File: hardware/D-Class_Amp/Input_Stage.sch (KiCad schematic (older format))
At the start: 19 parts

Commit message: edited input filter ground, created schematic for the SPWM generator
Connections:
- net labels removed: GND
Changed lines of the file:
@@
 $Descr A4 11693 8268
 encoding utf-8
-Sheet 1 1
+Sheet 2 5
 Title "D-Class Input Filter"
 Date "2021-07-31"
@@
 	8250 3600 8250 3550
 Connection ~ 8250 3600
-$Comp
-L power:GND #PWR?
-U 1 1 610999BC
-P 7550 3950
-F 0 "#PWR?" H 7550 3700 50  0001 C CNN
-F 1 "GND" H 7555 3777 50  0000 C CNN
-F 2 "" H 7550 3950 50  0001 C CNN
-F 3 "" H 7550 3950 50  0001 C CNN
-	1    7550 3950
-	1    0    0    -1
-$EndComp
-$Comp
-L power:GND #PWR?
-U 1 1 61099C7B
-P 8250 3950
-F 0 "#PWR?" H 8250 3700 50  0001 C CNN
-F 1 "GND" H 8255 3777 50  0000 C CNN
-F 2 "" H 8250 3950 50  0001 C CNN
-F 3 "" H 8250 3950 50  0001 C CNN
-	1    8250 3950
-	1    0    0    -1
-$EndComp
 Text HLabel 2600 3200 0    50   Input ~ 0
 SIG_IN
@@
 Text Label 3900 4650 0    50   ~ 0
 C_OUT
-Text HLabel 6650 4550 2    50   Input ~ 0
+Text HLabel 6650 4550 2    50   Output ~ 0
 FILT_OUT
 Wire Wire Line
@@
 	1    0    0    -1
 $EndComp
+$Comp
+L power:GNDS #PWR?
+U 1 1 61096DF3
+P 7550 3950
+F 0 "#PWR?" H 7550 3700 50  0001 C CNN
+F 1 "GNDS" H 7555 3777 50  0000 C CNN
+F 2 "" H 7550 3950 50  0001 C CNN
+F 3 "" H 7550 3950 50  0001 C CNN
+	1    7550 3950
+	1    0    0    -1
+$EndComp
+$Comp
+L power:GNDS #PWR?
+U 1 1 61097302
+P 8250 3950
+F 0 "#PWR?" H 8250 3700 50  0001 C CNN
+F 1 "GNDS" H 8255 3777 50  0000 C CNN
+F 2 "" H 8250 3950 50  0001 C CNN
+F 3 "" H 8250 3950 50  0001 C CNN
+	1    8250 3950
+	1    0    0    -1
+$EndComp

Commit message: edits
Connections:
- net labels added: +5V, -5V
- net labels removed: +3.3V, -3V3
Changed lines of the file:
@@
-$EndComp
-$Comp
-L power:+3.3V #PWR?
-U 1 1 610DB258
-P 8250 3550
-F 0 "#PWR?" H 8250 3400 50  0001 C CNN
-F 1 "+3.3V" H 8265 3723 50  0000 C CNN
-F 2 "" H 8250 3550 50  0001 C CNN
-F 3 "" H 8250 3550 50  0001 C CNN
-	1    8250 3550
-	1    0    0    -1
-$EndComp
-$Comp
-L power:-3V3 #PWR?
-U 1 1 610DB7DD
-P 7550 3550
-F 0 "#PWR?" H 7550 3650 50  0001 C CNN
-F 1 "-3V3" H 7565 3723 50  0000 C CNN
-F 2 "" H 7550 3550 50  0001 C CNN
-F 3 "" H 7550 3550 50  0001 C CNN
-	1    7550 3550
-	1    0    0    -1
 $EndComp
 $Comp
@@
 	1    0    0    -1
 $EndComp
+$Comp
+L power:-5V #PWR?
+U 1 1 611D5337
+P 7550 3550
+F 0 "#PWR?" H 7550 3650 50  0001 C CNN
+F 1 "-5V" H 7565 3723 50  0000 C CNN
+F 2 "" H 7550 3550 50  0001 C CNN
+F 3 "" H 7550 3550 50  0001 C CNN
+	1    7550 3550
+	1    0    0    -1
+$EndComp
+$Comp
+L power:+5V #PWR?
+U 1 1 611D5A3A
+P 8250 3550
+F 0 "#PWR?" H 8250 3400 50  0001 C CNN
+F 1 "+5V" H 8265 3723 50  0000 C CNN
+F 2 "" H 8250 3550 50  0001 C CNN
+F 3 "" H 8250 3550 50  0001 C CNN
+	1    8250 3550
+	1    0    0    -1
+$EndComp

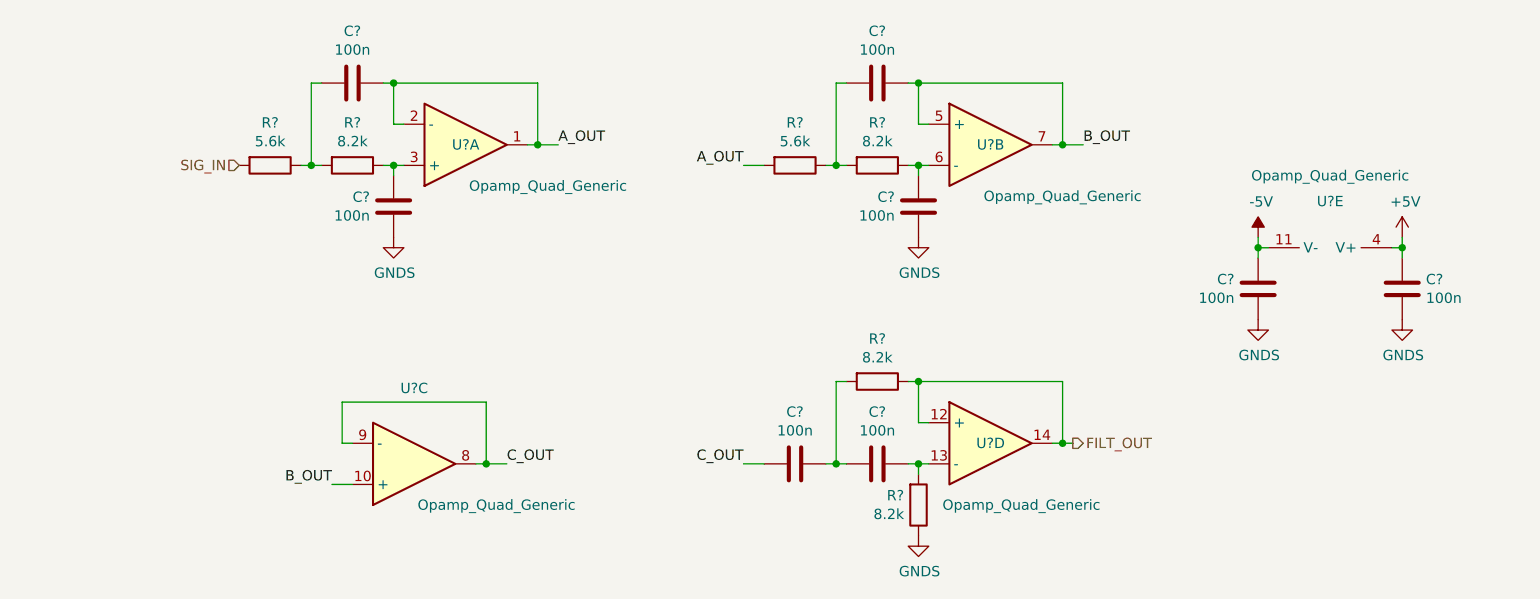
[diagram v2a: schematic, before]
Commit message: Selected Op-Amp for input stage and labelled parts
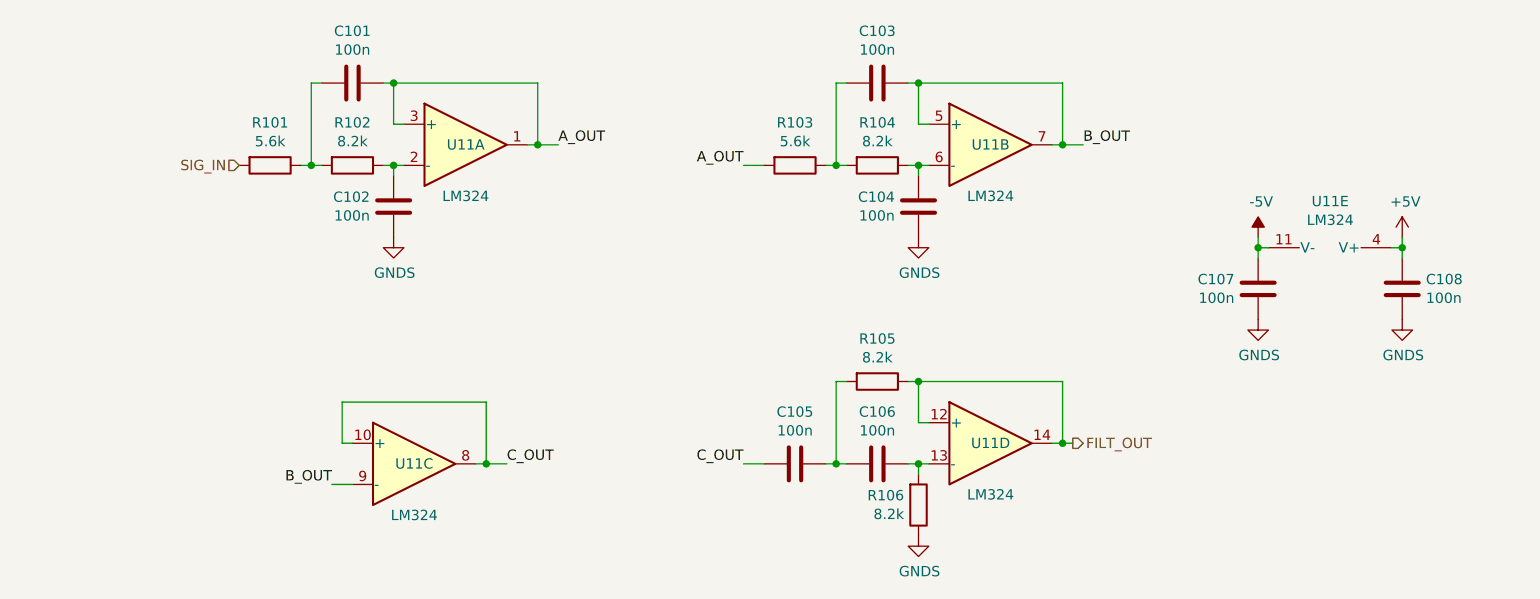
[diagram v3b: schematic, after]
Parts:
- removed U? (x5): Opamp_Quad_Generic, symbol Device:Opamp_Quad_Generic
- added U11: LM324, symbol Amplifier_Operational:LM324
- gave numbers to parts that had none: 14
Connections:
- net +5V: now also U11.4 (V+)
- net -5V: now also U11.11 (V-)
- net A_OUT: now also U11.1, U11.3 (+)
- net B_OUT: now also U11.5 (+), U11.7, U11.9 (-)
- net C_OUT: now also U11.10 (+), U11.8
- net FILT_OUT: now also U11.12 (+), U11.14
- net at C102.2, R102.1: now also U11.2 (-)
- net at C104.2, R104.1: now also U11.6 (-)
- net at C106.1, R106.2: now also U11.13 (-)
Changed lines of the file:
@@
 $Descr A4 11693 8268
 encoding utf-8
-Sheet 2 5
+Sheet 1 1
 Title "D-Class Input Filter"
 Date "2021-07-31"
@@
 $EndDescr
 $Comp
-L Device:Opamp_Quad_Generic U?
-U 2 1 6104ADDA
-P 6250 3100
-F 0 "U?" H 6250 3100 50  0000 C CNN
-F 1 "Opamp_Quad_Generic" H 6600 2850 50  0000 C CNN
-F 2 "" H 6250 3100 50  0001 C CNN
-F 3 "~" H 6250 3100 50  0001 C CNN
-	2    6250 3100
-	1    0    0    -1
-$EndComp
-$Comp
-L Device:Opamp_Quad_Generic U?
-U 3 1 6104B460
-P 3450 4650
-F 0 "U?" H 3450 4283 50  0000 C CNN
-F 1 "Opamp_Quad_Generic" H 3850 4850 50  0000 C CNN
-F 2 "" H 3450 4650 50  0001 C CNN
-F 3 "~" H 3450 4650 50  0001 C CNN
-	3    3450 4650
-	1    0    0    1
-$EndComp
-$Comp
-L Device:Opamp_Quad_Generic U?
-U 4 1 6104BA16
-P 6250 4550
-F 0 "U?" H 6250 4550 50  0000 C CNN
-F 1 "Opamp_Quad_Generic" H 6400 4250 50  0000 C CNN
-F 2 "" H 6250 4550 50  0001 C CNN
-F 3 "~" H 6250 4550 50  0001 C CNN
-	4    6250 4550
-	1    0    0    -1
-$EndComp
-$Comp
-L Device:Opamp_Quad_Generic U?
-U 5 1 6104C141
-P 7900 3700
-F 0 "U?" V 7575 3700 50  0000 C CNN
-F 1 "Opamp_Quad_Generic" V 7450 3700 50  0000 C CNN
-F 2 "" H 7900 3700 50  0001 C CNN
-F 3 "~" H 7900 3700 50  0001 C CNN
-	5    7900 3700
-	0    1    1    0
-$EndComp
-$Comp
-L Device:Opamp_Quad_Generic U?
-U 1 1 6104A90C
-P 3700 3100
-F 0 "U?" H 3700 3100 50  0000 C CNN
-F 1 "Opamp_Quad_Generic" H 4100 3300 50  0000 C CNN
-F 2 "" H 3700 3100 50  0001 C CNN
-F 3 "~" H 3700 3100 50  0001 C CNN
-	1    3700 3100
-	1    0    0    1
-$EndComp
-$Comp
-L Device:R R?
+L Device:R R101
 U 1 1 61051550
 P 2750 3200
-F 0 "R?" V 2543 3200 50  0000 C CNN
+F 0 "R101" V 2543 3200 50  0000 C CNN
 F 1 "5.6k" V 2634 3200 50  0000 C CNN
 F 2 "" V 2680 3200 50  0001 C CNN
@@
 $EndComp
 $Comp
-L Device:C C?
+L Device:C C102
 U 1 1 610518F4
 P 3350 3400
-F 0 "C?" H 3235 3354 50  0000 R CNN
+F 0 "C102" H 3235 3354 50  0000 R CNN
 F 1 "100n" H 3235 3445 50  0000 R CNN
 F 2 "" H 3388 3250 50  0001 C CNN
@@
 $EndComp
 $Comp
-L Device:R R?
+L Device:R R102
 U 1 1 61052760
 P 3150 3200
-F 0 "R?" V 2943 3200 50  0000 C CNN
+F 0 "R102" V 2943 3200 50  0000 C CNN
 F 1 "8.2k" V 3034 3200 50  0000 C CNN
 F 2 "" V 3080 3200 50  0001 C CNN
@@
 	4050 3100 4000 3100
 $Comp
-L Device:C C?
+L Device:C C101
 U 1 1 6105C4D1
 P 3150 2800
-F 0 "C?" V 2898 2800 50  0000 C CNN
+F 0 "C101" V 2898 2800 50  0000 C CNN
 F 1 "100n" V 2989 2800 50  0000 C CNN
 F 2 "" H 3188 2650 50  0001 C CNN
@@
 	3350 2800 4050 2800
 $Comp
-L Device:R R?
+L Device:R R103
 U 1 1 6105F15E
 P 5300 3200
-F 0 "R?" V 5093 3200 50  0000 C CNN
+F 0 "R103" V 5093 3200 50  0000 C CNN
 F 1 "5.6k" V 5184 3200 50  0000 C CNN
 F 2 "" V 5230 3200 50  0001 C CNN
@@
 $EndComp
 $Comp
-L Device:C C?
+L Device:C C104
 U 1 1 6105F164
 P 5900 3400
-F 0 "C?" H 5785 3354 50  0000 R CNN
+F 0 "C104" H 5785 3354 50  0000 R CNN
 F 1 "100n" H 5785 3445 50  0000 R CNN
 F 2 "" H 5938 3250 50  0001 C CNN
@@
 $EndComp
 $Comp
-L Device:R R?
+L Device:R R104
 U 1 1 6105F16A
 P 5700 3200
-F 0 "R?" V 5493 3200 50  0000 C CNN
+F 0 "R104" V 5493 3200 50  0000 C CNN
 F 1 "8.2k" V 5584 3200 50  0000 C CNN
 F 2 "" V 5630 3200 50  0001 C CNN
@@
 	6600 3100 6550 3100
 $Comp
-L Device:C C?
+L Device:C C103
 U 1 1 6105F17C
 P 5700 2800
-F 0 "C?" V 5448 2800 50  0000 C CNN
+F 0 "C103" V 5448 2800 50  0000 C CNN
 F 1 "100n" V 5539 2800 50  0000 C CNN
 F 2 "" H 5738 2650 50  0001 C CNN
@@
 	3800 4650 3750 4650
 $Comp
-L Device:R R?
+L Device:R R106
 U 1 1 6106C181
 P 5900 4850
-F 0 "R?" H 5830 4804 50  0000 R CNN
+F 0 "R106" H 5830 4804 50  0000 R CNN
 F 1 "8.2k" H 5830 4895 50  0000 R CNN
 F 2 "" V 5830 4850 50  0001 C CNN
@@
 	5900 4650 5950 4650
 $Comp
-L Device:C C?
+L Device:C C106
 U 1 1 61078298
 P 5700 4650
-F 0 "C?" V 5448 4650 50  0000 C CNN
+F 0 "C106" V 5448 4650 50  0000 C CNN
 F 1 "100n" V 5539 4650 50  0000 C CNN
 F 2 "" H 5738 4500 50  0001 C CNN
@@
 $EndComp
 $Comp
-L Device:C C?
+L Device:C C105
 U 1 1 61078600
 P 5300 4650
-F 0 "C?" V 5048 4650 50  0000 C CNN
+F 0 "C105" V 5048 4650 50  0000 C CNN
 F 1 "100n" V 5139 4650 50  0000 C CNN
 F 2 "" H 5338 4500 50  0001 C CNN
@@
 Connection ~ 5900 4650
 $Comp
-L Device:R R?
+L Device:R R105
 U 1 1 6107C170
 P 5700 4250
-F 0 "R?" V 5493 4250 50  0000 C CNN
+F 0 "R105" V 5493 4250 50  0000 C CNN
 F 1 "8.2k" V 5584 4250 50  0000 C CNN
 F 2 "" V 5630 4250 50  0001 C CNN
@@
 Connection ~ 5900 4250
 $Comp
-L Device:C C?
+L Device:C C107
 U 1 1 6108D745
 P 7550 3800
-F 0 "C?" H 7435 3754 50  0000 R CNN
+F 0 "C107" H 7435 3754 50  0000 R CNN
 F 1 "100n" H 7435 3845 50  0000 R CNN
 F 2 "" H 7588 3650 50  0001 C CNN
@@
 $EndComp
 $Comp
-L Device:C C?
+L Device:C C108
 U 1 1 61092744
 P 8250 3800
-F 0 "C?" H 8135 3846 50  0000 R CNN
+F 0 "C108" H 8135 3846 50  0000 R CNN
 F 1 "100n" H 8135 3755 50  0000 R CNN
 F 2 "" H 8288 3650 50  0001 C CNN
@@
 	1    0    0    -1
 $EndComp
+$Comp
+L Amplifier_Operational:LM324 U11
+U 1 1 61050744
+P 3700 3100
+F 0 "U11" H 3700 3100 50  0000 C CNN
+F 1 "LM324" H 3700 2850 50  0000 C CNN
+F 2 "" H 3650 3200 50  0001 C CNN
+F 3 "http://www.ti.com/lit/ds/symlink/lm2902-n.pdf" H 3750 3300 50  0001 C CNN
+	1    3700 3100
+	1    0    0    -1
+$EndComp
+$Comp
+L Amplifier_Operational:LM324 U11
+U 2 1 6105141E
+P 6250 3100
+F 0 "U11" H 6250 3100 50  0000 C CNN
+F 1 "LM324" H 6250 2850 50  0000 C CNN
+F 2 "" H 6200 3200 50  0001 C CNN
+F 3 "http://www.ti.com/lit/ds/symlink/lm2902-n.pdf" H 6300 3300 50  0001 C CNN
+	2    6250 3100
+	1    0    0    -1
+$EndComp
+$Comp
+L Amplifier_Operational:LM324 U11
+U 3 1 61052C39
+P 3450 4650
+F 0 "U11" H 3450 4650 50  0000 C CNN
+F 1 "LM324" H 3450 4400 50  0000 C CNN
+F 2 "" H 3400 4750 50  0001 C CNN
+F 3 "http://www.ti.com/lit/ds/symlink/lm2902-n.pdf" H 3500 4850 50  0001 C CNN
+	3    3450 4650
+	1    0    0    -1
+$EndComp
+$Comp
+L Amplifier_Operational:LM324 U11
+U 4 1 61053F29
+P 6250 4550
+F 0 "U11" H 6250 4550 50  0000 C CNN
+F 1 "LM324" H 6250 4300 50  0000 C CNN
+F 2 "" H 6200 4650 50  0001 C CNN
+F 3 "http://www.ti.com/lit/ds/symlink/lm2902-n.pdf" H 6300 4750 50  0001 C CNN
+	4    6250 4550
+	1    0    0    -1
+$EndComp
+$Comp
+L Amplifier_Operational:LM324 U11
+U 5 1 610564DD
+P 7900 3700
+F 0 "U11" V 7575 3700 50  0000 C CNN
+F 1 "LM324" V 7666 3700 50  0000 C CNN
+F 2 "" H 7850 3800 50  0001 C CNN
+F 3 "http://www.ti.com/lit/ds/symlink/lm2902-n.pdf" H 7950 3900 50  0001 C CNN
+	5    7900 3700
+	0    1    1    0
+$EndComp
 $EndSCHEMATC

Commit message: Set footprints for the input stage components.
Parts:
- C101, C102, C103, C104, C105, C106, C107, C108: footprint (none) -> Capacitor_SMD:C_0805_2012Metric_Pad1.18x1.45mm_HandSolder
- R101, R102, R103, R104, R105, R106: footprint (none) -> Resistor_SMD:R_0805_2012Metric_Pad1.20x1.40mm_HandSolder
- U11: footprint (none) -> Package_SO:SOIC-14_3.9x8.7mm_P1.27mm
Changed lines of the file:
@@
 F 0 "R101" V 2543 3200 50  0000 C CNN
 F 1 "5.6k" V 2634 3200 50  0000 C CNN
-F 2 "" V 2680 3200 50  0001 C CNN
+F 2 "Resistor_SMD:R_0805_2012Metric_Pad1.20x1.40mm_HandSolder" V 2680 3200 50  0001 C CNN
 F 3 "~" H 2750 3200 50  0001 C CNN
 	1    2750 3200
@@
 F 0 "C102" H 3235 3354 50  0000 R CNN
 F 1 "100n" H 3235 3445 50  0000 R CNN
-F 2 "" H 3388 3250 50  0001 C CNN
+F 2 "Capacitor_SMD:C_0805_2012Metric_Pad1.18x1.45mm_HandSolder" H 3388 3250 50  0001 C CNN
 F 3 "~" H 3350 3400 50  0001 C CNN
 	1    3350 3400
@@
 F 0 "R102" V 2943 3200 50  0000 C CNN
 F 1 "8.2k" V 3034 3200 50  0000 C CNN
-F 2 "" V 3080 3200 50  0001 C CNN
+F 2 "Resistor_SMD:R_0805_2012Metric_Pad1.20x1.40mm_HandSolder" V 3080 3200 50  0001 C CNN
 F 3 "~" H 3150 3200 50  0001 C CNN
 	1    3150 3200
@@
 F 0 "C101" V 2898 2800 50  0000 C CNN
 F 1 "100n" V 2989 2800 50  0000 C CNN
-F 2 "" H 3188 2650 50  0001 C CNN
+F 2 "Capacitor_SMD:C_0805_2012Metric_Pad1.18x1.45mm_HandSolder" H 3188 2650 50  0001 C CNN
 F 3 "~" H 3150 2800 50  0001 C CNN
 	1    3150 2800
@@
 F 0 "R103" V 5093 3200 50  0000 C CNN
 F 1 "5.6k" V 5184 3200 50  0000 C CNN
-F 2 "" V 5230 3200 50  0001 C CNN
+F 2 "Resistor_SMD:R_0805_2012Metric_Pad1.20x1.40mm_HandSolder" V 5230 3200 50  0001 C CNN
 F 3 "~" H 5300 3200 50  0001 C CNN
 	1    5300 3200
@@
 F 0 "C104" H 5785 3354 50  0000 R CNN
 F 1 "100n" H 5785 3445 50  0000 R CNN
-F 2 "" H 5938 3250 50  0001 C CNN
+F 2 "Capacitor_SMD:C_0805_2012Metric_Pad1.18x1.45mm_HandSolder" H 5938 3250 50  0001 C CNN
 F 3 "~" H 5900 3400 50  0001 C CNN
 	1    5900 3400
@@
 F 0 "R104" V 5493 3200 50  0000 C CNN
 F 1 "8.2k" V 5584 3200 50  0000 C CNN
-F 2 "" V 5630 3200 50  0001 C CNN
+F 2 "Resistor_SMD:R_0805_2012Metric_Pad1.20x1.40mm_HandSolder" V 5630 3200 50  0001 C CNN
 F 3 "~" H 5700 3200 50  0001 C CNN
 	1    5700 3200
@@
 F 0 "C103" V 5448 2800 50  0000 C CNN
 F 1 "100n" V 5539 2800 50  0000 C CNN
-F 2 "" H 5738 2650 50  0001 C CNN
+F 2 "Capacitor_SMD:C_0805_2012Metric_Pad1.18x1.45mm_HandSolder" H 5738 2650 50  0001 C CNN
 F 3 "~" H 5700 2800 50  0001 C CNN
 	1    5700 2800
@@
 F 0 "R106" H 5830 4804 50  0000 R CNN
 F 1 "8.2k" H 5830 4895 50  0000 R CNN
-F 2 "" V 5830 4850 50  0001 C CNN
+F 2 "Resistor_SMD:R_0805_2012Metric_Pad1.20x1.40mm_HandSolder" V 5830 4850 50  0001 C CNN
 F 3 "~" H 5900 4850 50  0001 C CNN
 	1    5900 4850
@@
 F 0 "C106" V 5448 4650 50  0000 C CNN
 F 1 "100n" V 5539 4650 50  0000 C CNN
-F 2 "" H 5738 4500 50  0001 C CNN
+F 2 "Capacitor_SMD:C_0805_2012Metric_Pad1.18x1.45mm_HandSolder" H 5738 4500 50  0001 C CNN
 F 3 "~" H 5700 4650 50  0001 C CNN
 	1    5700 4650
@@
 F 0 "C105" V 5048 4650 50  0000 C CNN
 F 1 "100n" V 5139 4650 50  0000 C CNN
-F 2 "" H 5338 4500 50  0001 C CNN
+F 2 "Capacitor_SMD:C_0805_2012Metric_Pad1.18x1.45mm_HandSolder" H 5338 4500 50  0001 C CNN
 F 3 "~" H 5300 4650 50  0001 C CNN
 	1    5300 4650
@@
 F 0 "R105" V 5493 4250 50  0000 C CNN
 F 1 "8.2k" V 5584 4250 50  0000 C CNN
-F 2 "" V 5630 4250 50  0001 C CNN
+F 2 "Resistor_SMD:R_0805_2012Metric_Pad1.20x1.40mm_HandSolder" V 5630 4250 50  0001 C CNN
 F 3 "~" H 5700 4250 50  0001 C CNN
 	1    5700 4250
@@
 F 0 "C107" H 7435 3754 50  0000 R CNN
 F 1 "100n" H 7435 3845 50  0000 R CNN
-F 2 "" H 7588 3650 50  0001 C CNN
+F 2 "Capacitor_SMD:C_0805_2012Metric_Pad1.18x1.45mm_HandSolder" H 7588 3650 50  0001 C CNN
 F 3 "~" H 7550 3800 50  0001 C CNN
 	1    7550 3800
@@
 F 0 "C108" H 8135 3846 50  0000 R CNN
 F 1 "100n" H 8135 3755 50  0000 R CNN
-F 2 "" H 8288 3650 50  0001 C CNN
+F 2 "Capacitor_SMD:C_0805_2012Metric_Pad1.18x1.45mm_HandSolder" H 8288 3650 50  0001 C CNN
 F 3 "~" H 8250 3800 50  0001 C CNN
 	1    8250 3800
@@
 C_OUT
 $Comp
-L power:GNDS #PWR?
+L power:GNDS #PWR0101
 U 1 1 610D7973
 P 3350 3550
-F 0 "#PWR?" H 3350 3300 50  0001 C CNN
+F 0 "#PWR0101" H 3350 3300 50  0001 C CNN
 F 1 "GNDS" H 3355 3377 50  0000 C CNN
 F 2 "" H 3350 3550 50  0001 C CNN
@@
 $EndComp
 $Comp
-L power:GNDS #PWR?
+L power:GNDS #PWR0102
 U 1 1 610D9C89
 P 5900 3550
-F 0 "#PWR?" H 5900 3300 50  0001 C CNN
+F 0 "#PWR0102" H 5900 3300 50  0001 C CNN
 F 1 "GNDS" H 5905 3377 50  0000 C CNN
 F 2 "" H 5900 3550 50  0001 C CNN
@@
 $EndComp
 $Comp
-L power:GNDS #PWR?
+L power:GNDS #PWR0103
 U 1 1 610DA117
 P 5900 5000
-F 0 "#PWR?" H 5900 4750 50  0001 C CNN
+F 0 "#PWR0103" H 5900 4750 50  0001 C CNN
 F 1 "GNDS" H 5905 4827 50  0000 C CNN
 F 2 "" H 5900 5000 50  0001 C CNN
@@
 $EndComp
 $Comp
-L power:GNDS #PWR?
+L power:GNDS #PWR0104
 U 1 1 61096DF3
 P 7550 3950
-F 0 "#PWR?" H 7550 3700 50  0001 C CNN
+F 0 "#PWR0104" H 7550 3700 50  0001 C CNN
 F 1 "GNDS" H 7555 3777 50  0000 C CNN
 F 2 "" H 7550 3950 50  0001 C CNN
@@
 $EndComp
 $Comp
-L power:GNDS #PWR?
+L power:GNDS #PWR0105
 U 1 1 61097302
 P 8250 3950
-F 0 "#PWR?" H 8250 3700 50  0001 C CNN
+F 0 "#PWR0105" H 8250 3700 50  0001 C CNN
 F 1 "GNDS" H 8255 3777 50  0000 C CNN
 F 2 "" H 8250 3950 50  0001 C CNN
@@
 $EndComp
 $Comp
-L power:-5V #PWR?
+L power:-5V #PWR0106
 U 1 1 611D5337
 P 7550 3550
-F 0 "#PWR?" H 7550 3650 50  0001 C CNN
+F 0 "#PWR0106" H 7550 3650 50  0001 C CNN
 F 1 "-5V" H 7565 3723 50  0000 C CNN
 F 2 "" H 7550 3550 50  0001 C CNN
@@
 $EndComp
 $Comp
-L power:+5V #PWR?
+L power:+5V #PWR0107
 U 1 1 611D5A3A
 P 8250 3550
-F 0 "#PWR?" H 8250 3400 50  0001 C CNN
+F 0 "#PWR0107" H 8250 3400 50  0001 C CNN
 F 1 "+5V" H 8265 3723 50  0000 C CNN
 F 2 "" H 8250 3550 50  0001 C CNN
@@
 F 0 "U11" H 3700 3100 50  0000 C CNN
 F 1 "LM324" H 3700 2850 50  0000 C CNN
-F 2 "" H 3650 3200 50  0001 C CNN
+F 2 "Package_SO:SOIC-14_3.9x8.7mm_P1.27mm" H 3650 3200 50  0001 C CNN
 F 3 "http://www.ti.com/lit/ds/symlink/lm2902-n.pdf" H 3750 3300 50  0001 C CNN
 	1    3700 3100
@@
 F 0 "U11" H 6250 3100 50  0000 C CNN
 F 1 "LM324" H 6250 2850 50  0000 C CNN
-F 2 "" H 6200 3200 50  0001 C CNN
+F 2 "Package_SO:SOIC-14_3.9x8.7mm_P1.27mm" H 6200 3200 50  0001 C CNN
 F 3 "http://www.ti.com/lit/ds/symlink/lm2902-n.pdf" H 6300 3300 50  0001 C CNN
 	2    6250 3100
@@
 F 0 "U11" H 3450 4650 50  0000 C CNN
 F 1 "LM324" H 3450 4400 50  0000 C CNN
-F 2 "" H 3400 4750 50  0001 C CNN
+F 2 "Package_SO:SOIC-14_3.9x8.7mm_P1.27mm" H 3400 4750 50  0001 C CNN
 F 3 "http://www.ti.com/lit/ds/symlink/lm2902-n.pdf" H 3500 4850 50  0001 C CNN
 	3    3450 4650
@@
 F 0 "U11" H 6250 4550 50  0000 C CNN
 F 1 "LM324" H 6250 4300 50  0000 C CNN
-F 2 "" H 6200 4650 50  0001 C CNN
+F 2 "Package_SO:SOIC-14_3.9x8.7mm_P1.27mm" H 6200 4650 50  0001 C CNN
 F 3 "http://www.ti.com/lit/ds/symlink/lm2902-n.pdf" H 6300 4750 50  0001 C CNN
 	4    6250 4550
@@
 F 0 "U11" V 7575 3700 50  0000 C CNN
 F 1 "LM324" V 7666 3700 50  0000 C CNN
-F 2 "" H 7850 3800 50  0001 C CNN
+F 2 "Package_SO:SOIC-14_3.9x8.7mm_P1.27mm" H 7850 3800 50  0001 C CNN
 F 3 "http://www.ti.com/lit/ds/symlink/lm2902-n.pdf" H 7950 3900 50  0001 C CNN
 	5    7900 3700
